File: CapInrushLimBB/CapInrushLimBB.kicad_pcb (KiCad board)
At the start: 2 copper layers, 56.5 x 34.9 mm, 29 parts, among them J1 Screw_Terminal_01x02, J2 Screw_Terminal_01x02, K1 G5LE-1A, Q1 MPSA42, Q2 IRF9540N, Q3 MPSA42, Q4 Q_PMOS_GDSD

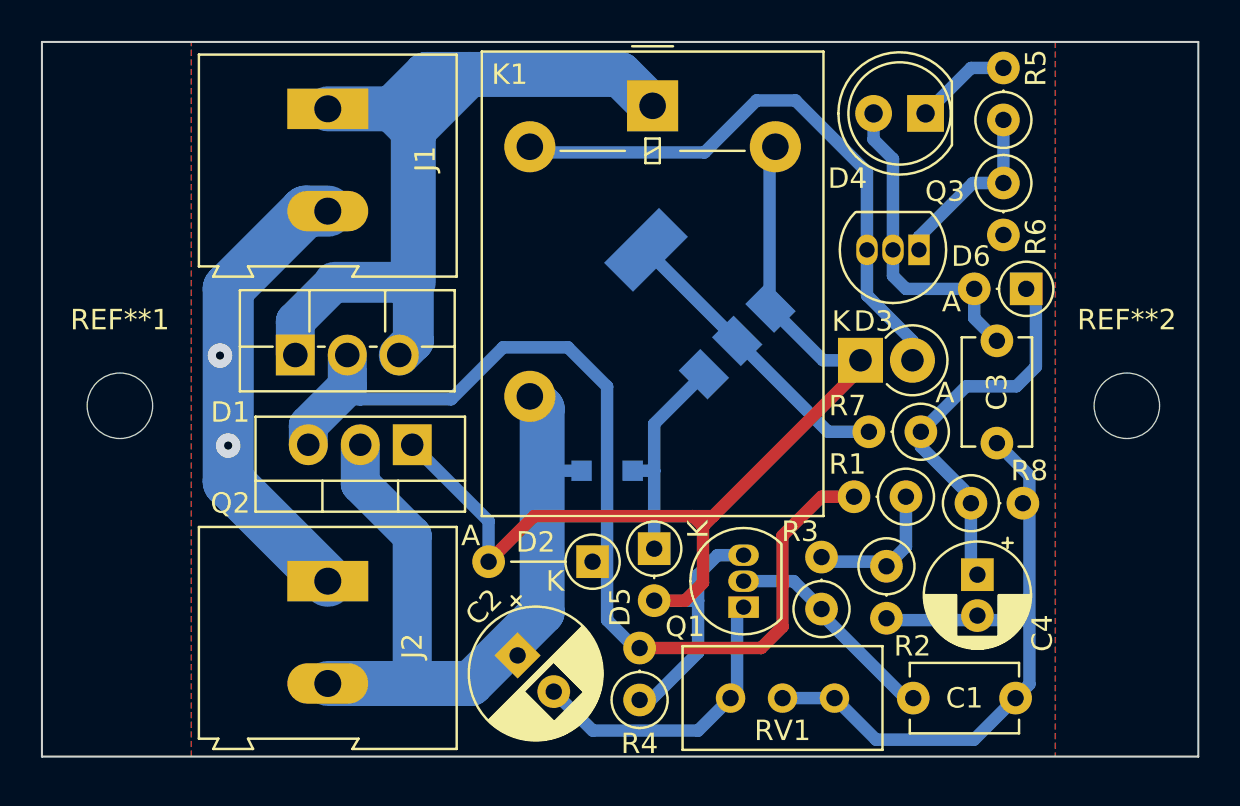
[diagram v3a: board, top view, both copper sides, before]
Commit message: Tweaked BJT footprint (custom) to increase clearance and tweaked track positions accordingly.
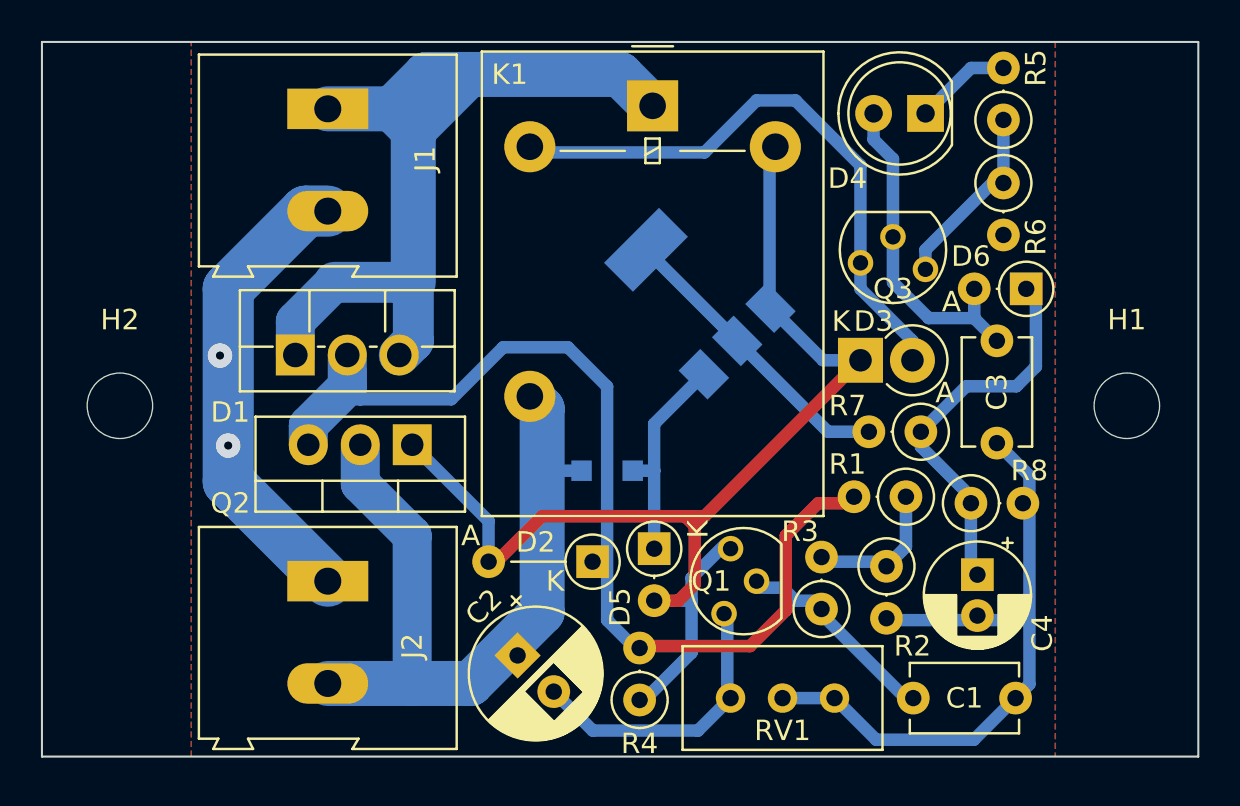
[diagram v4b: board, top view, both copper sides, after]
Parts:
- removed REF**1, REF**2: MountingHole_3.2mm_M3, MountingHole:MountingHole_3.2mm_M3
- added H1: MountingHole, MountingHole:MountingHole_3.2mm_M3, F.Cu at (260.0, 143.2)
- added H2: MountingHole, MountingHole:MountingHole_3.2mm_M3, F.Cu at (210.8, 143.2)
- Q1, Q3: footprint Package_TO_SOT_THT:TO-92_Inline -> CapInrushLim:TO-92_Inline
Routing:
- net /RLCoilHigh: track 63.0 -> 61.0 mm
- net Net-(C1-Pad1): track 10.8 -> 9.62 mm
- net Net-(C3-Pad2): track 15.6 -> 16.3 mm
- net Net-(C2-Pad2): track 15.0 -> 14.3 mm
- net /PolProtect: track 52.2 -> 51.6 mm

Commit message: Slight track tweak following assembly.
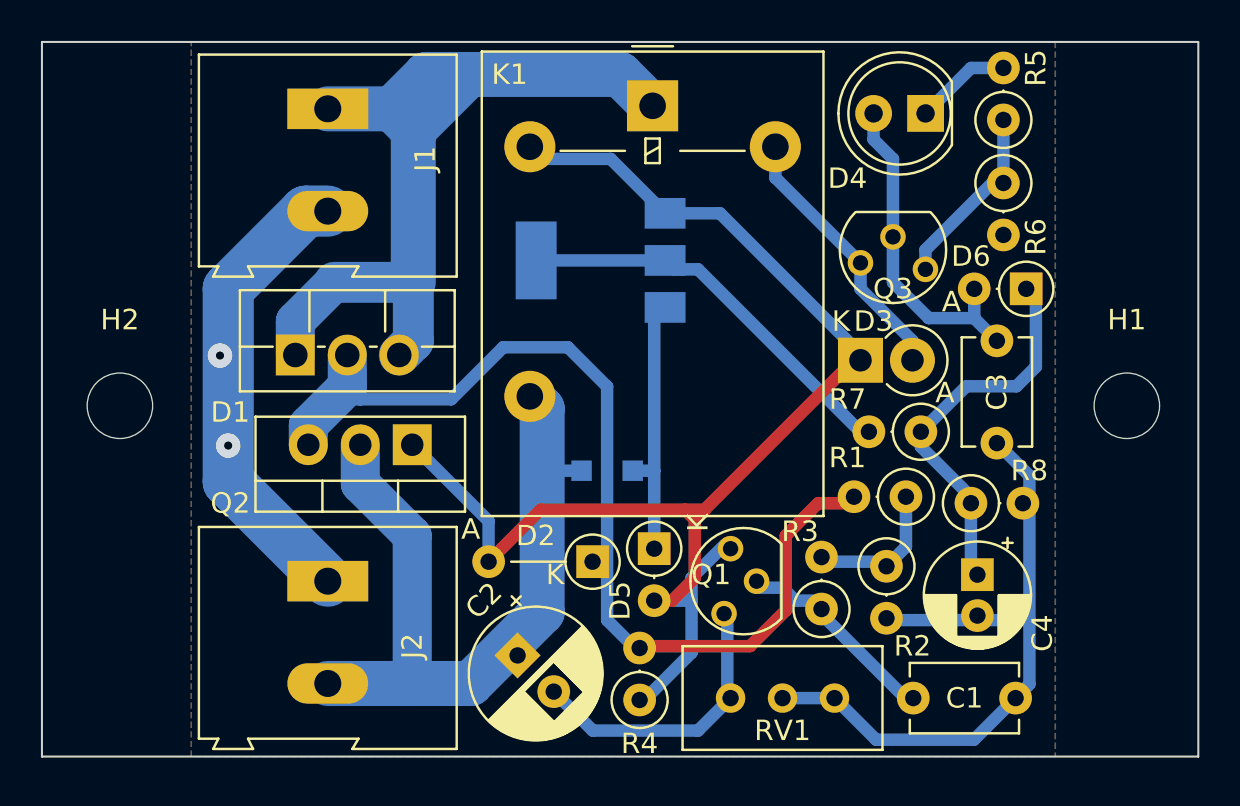
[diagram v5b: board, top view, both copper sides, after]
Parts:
- Q4: value Q_PMOS_GDSD -> BSP230 300V 0.21A
- moved Q4 4.76 mm to (234.3, 136.1), turned to 180 degrees
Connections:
- K1 pad 2: /RLCoilLow -> /RLCoilHigh
- K1 pad 4: /RLCoilHigh -> /RLCoilLow
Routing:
- net /RLCoilLow: track 29.2 -> 13.2 mm
- net /RLCoilHigh: track 61.0 -> 67.9 mm
- net Net-(Q4-Pad2): track 14.6 -> 19.7 mm
- net Net-(D5-Pad1): track 10.6 -> 12.9 mm

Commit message: Updated to remove LED reference (use two diodes) and relayed out following update.
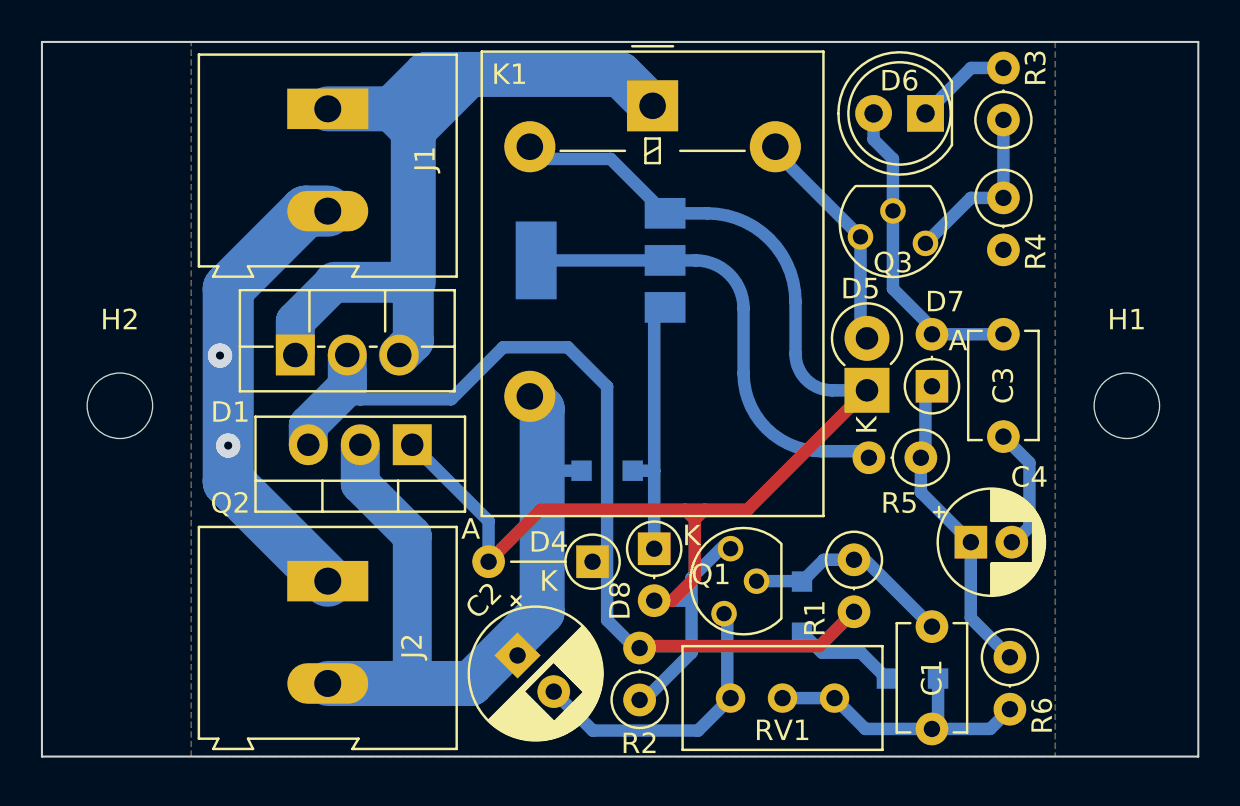
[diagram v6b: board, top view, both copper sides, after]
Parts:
- removed the R2 at (248.3, 151.0)
- removed the R3 at (245.1, 153.1)
- added D2: BAS16H, Diode_SMD:D_SOD-323_HandSoldering, B.Cu at (244.2, 153.0)
- added D3: BAS16H, Diode_SMD:D_SOD-323_HandSoldering, B.Cu at (249.6, 156.5)
- C1: value 220nF 50V -> 680nF 100V
- moved R6 7.76 mm to (254.3, 155.5), turned to -90 degrees
- moved D7 6.63 mm to (250.5, 142.2), turned to 90 degrees
- moved R1 3.99 mm to (246.7, 150.7), turned to -90 degrees
- moved C1 3.61 mm to (250.5, 154.0), turned to -90 degrees
- moved C4 1.62 mm to (252.4, 149.9), turned to 0 degrees
- moved D5 1.50 mm to (247.3, 142.4), turned to 90 degrees
- moved Q3 1.27 mm to (249.9, 134.3)
- moved R5 1.27 mm to (250.0, 145.7)
- moved R4 0.73 mm to (254.0, 133.0)
- moved C3 0.45 mm to (254.0, 144.7)
- renumbered D2 to D4, D3 to D5, D4 to D6, D6 to D7, D5 to D8, D7 to D9, R4 to R2, R5 to R3, R6 to R4, R7 to R5, R8 to R6
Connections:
- R1 pad 1: Net-(R1-Pad1) -> Net-(C1-Pad1)
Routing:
- net /Gnd: track 60.8 -> 48.2 mm
- net Net-(R1-Pad1): track 7.16 -> 0.00 mm
- net Net-(D2-Pad1): track 0.00 -> 5.08 mm
- net /PolProtect: track 51.6 -> 47.3 mm
- net Net-(C4-Pad1): track 19.0 -> 15.3 mm
- net Net-(Q4-Pad2): track 19.7 -> 22.7 mm
- net /RLCoilHigh: track 67.9 -> 70.6 mm
- net /RLCoilLow: track 13.2 -> 11.3 mm
- net Net-(C3-Pad2): track 16.3 -> 15.5 mm
- net Net-(Q3-Pad1): track 9.20 -> 8.54 mm
- net Net-(C1-Pad1): track 9.62 -> 10.2 mm

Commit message: Increased pad sizes on the TO92 footprint and tidied up the layout a tad.
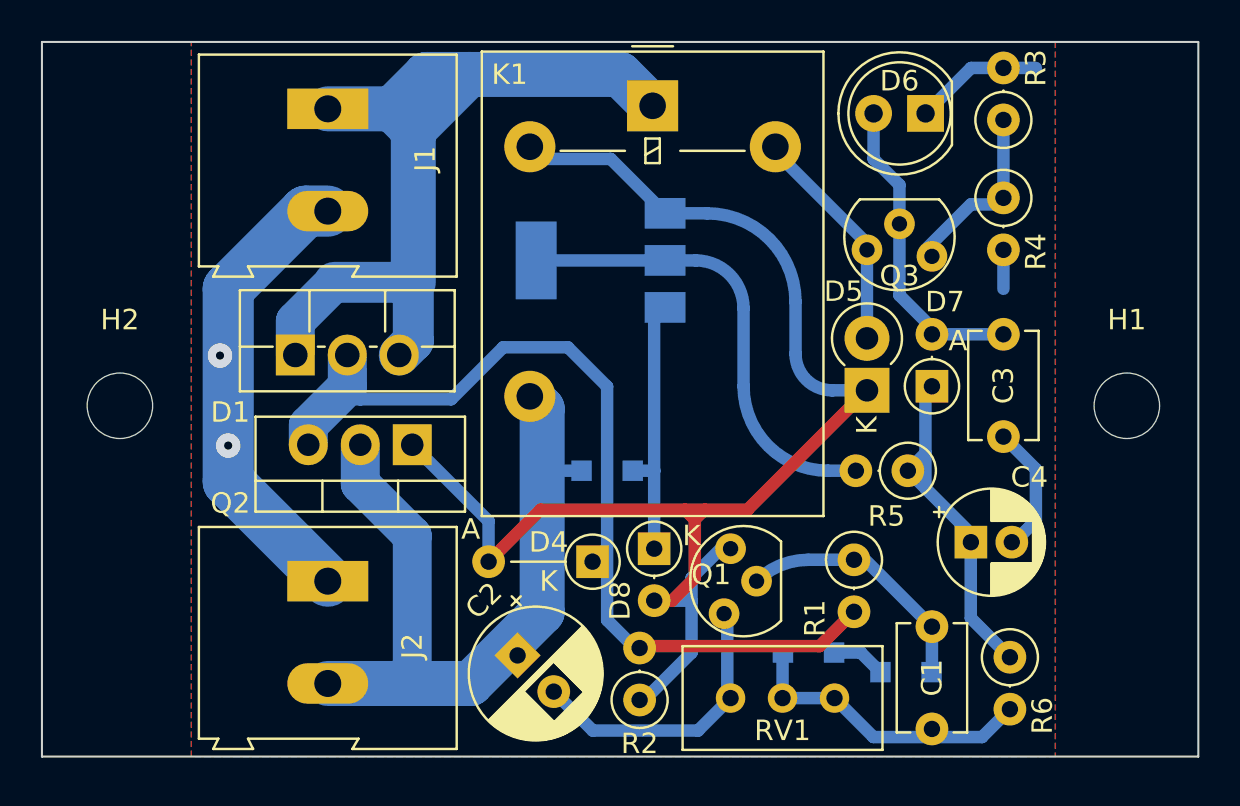
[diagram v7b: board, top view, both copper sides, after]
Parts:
- moved D2 5.99 mm to (249.2, 156.2), turned to 0 degrees
- moved D3 5.24 mm to (244.5, 155.3), turned to 0 degrees
- moved R5 0.90 mm to (249.3, 146.4)
- moved Q3 0.71 mm to (250.2, 134.9)
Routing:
- net /Gnd: track 48.2 -> 52.1 mm
- net Net-(D2-Pad1): track 5.08 -> 2.66 mm
- net Net-(C1-Pad1): track 10.2 -> 12.2 mm
- net Net-(C4-Pad1): track 15.3 -> 17.1 mm
- net Net-(C3-Pad2): track 15.5 -> 14.8 mm

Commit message: Layout tweaks.
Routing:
- net Net-(C1-Pad1): track 12.2 -> 12.8 mm
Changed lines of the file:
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@@
   (segment (start 222.5675 147.0025) (end 222.5675 145.258596) (width 1.905) (layer "B.Cu") (net 1))
   (segment (start 244.457853 150.72) (end 246.6975 150.72) (width 0.6096) (layer "B.Cu") (net 2))
+  (segment (start 247.24 150.72) (end 246.6975 150.72) (width 0.6096) (layer "B.Cu") (net 2))
   (segment (start 250.5075 153.9875) (end 250.5075 156.19) (width 0.6096) (layer "B.Cu") (net 2))
   (segment (start 250.5075 156.19) (end 250.4875 156.21) (width 0.6096) (layer "B.Cu") (net 2))
-  (segment (start 250.5075 153.9875) (end 247.015 150.495) (width 0.6096) (layer "B.Cu") (net 2))
+  (arc (start 250.5075 153.9875) (mid 249.550471 151.677029) (end 247.24 150.72) (width 0.6096) (layer "B.Cu") (net 2))
   (arc (start 241.935 151.765) (mid 243.092494 150.991587) (end 244.457853 150.72) (width 0.6096) (layer "B.Cu") (net 2))
   (segment (start 240.50625 157.32125) (end 240.665 157.48) (width 0.6096) (layer "B.Cu") (net 3))
@@
   (segment (start 242.855 130.7775) (end 242.855 130.5325) (width 0.6096) (layer "B.Cu") (net 8))
   (segment (start 247.3325 135.5725) (end 247.3325 135.255) (width 0.6096) (layer "B.Cu") (net 8))
-  (segment (start 254 133.0325) (end 254 133.35) (width 0.6096) (layer "B.Cu") (net 9))
+  (segment (start 250.5075 135.89) (end 250.825 135.89) (width 0.6096) (layer "B.Cu") (net 9))
+  (segment (start 253.6825 133.0325) (end 254 133.0325) (width 0.6096) (layer "B.Cu") (net 9))
   (segment (start 254 129.2225) (end 254 133.0325) (width 0.6096) (layer "B.Cu") (net 9))
-  (segment (start 252.4125 133.35) (end 250.19 135.5725) (width 0.6096) (layer "B.Cu") (net 9))
-  (segment (start 254 133.35) (end 252.4125 133.35) (width 0.6096) (layer "B.Cu") (net 9))
+  (segment (start 250.825 135.89) (end 253.6825 133.0325) (width 0.6096) (layer "B.Cu") (net 9))
   (segment (start 241.3 142.24) (end 241.3 138.43) (width 0.6096) (layer "B.Cu") (net 10))
   (segment (start 237.465 136.0875) (end 231.165 136.0875) (width 0.6096) (layer "B.Cu") (net 10))
